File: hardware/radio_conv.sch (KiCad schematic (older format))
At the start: 13 parts

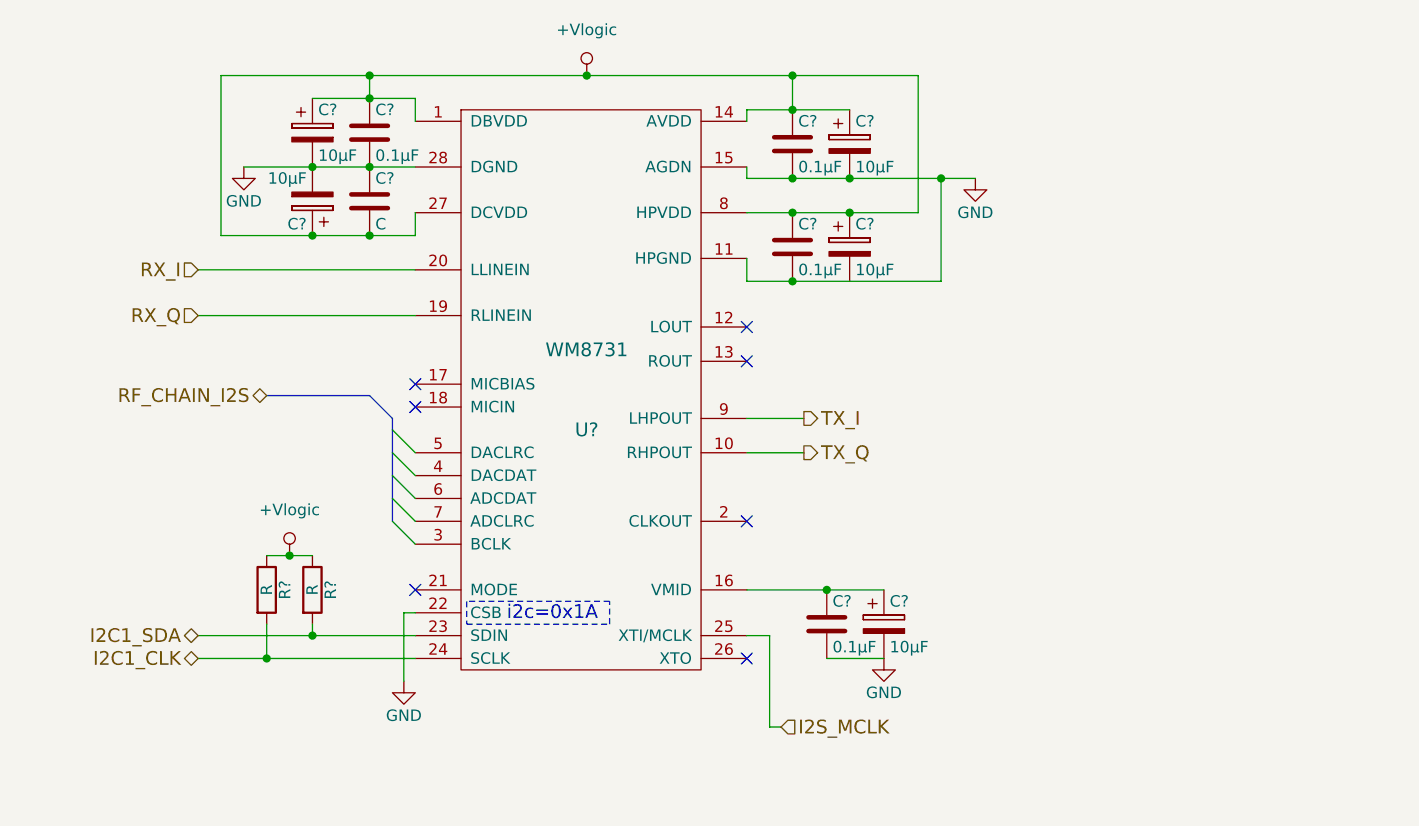
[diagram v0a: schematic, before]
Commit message: Added biases for RX and TX chains where needed
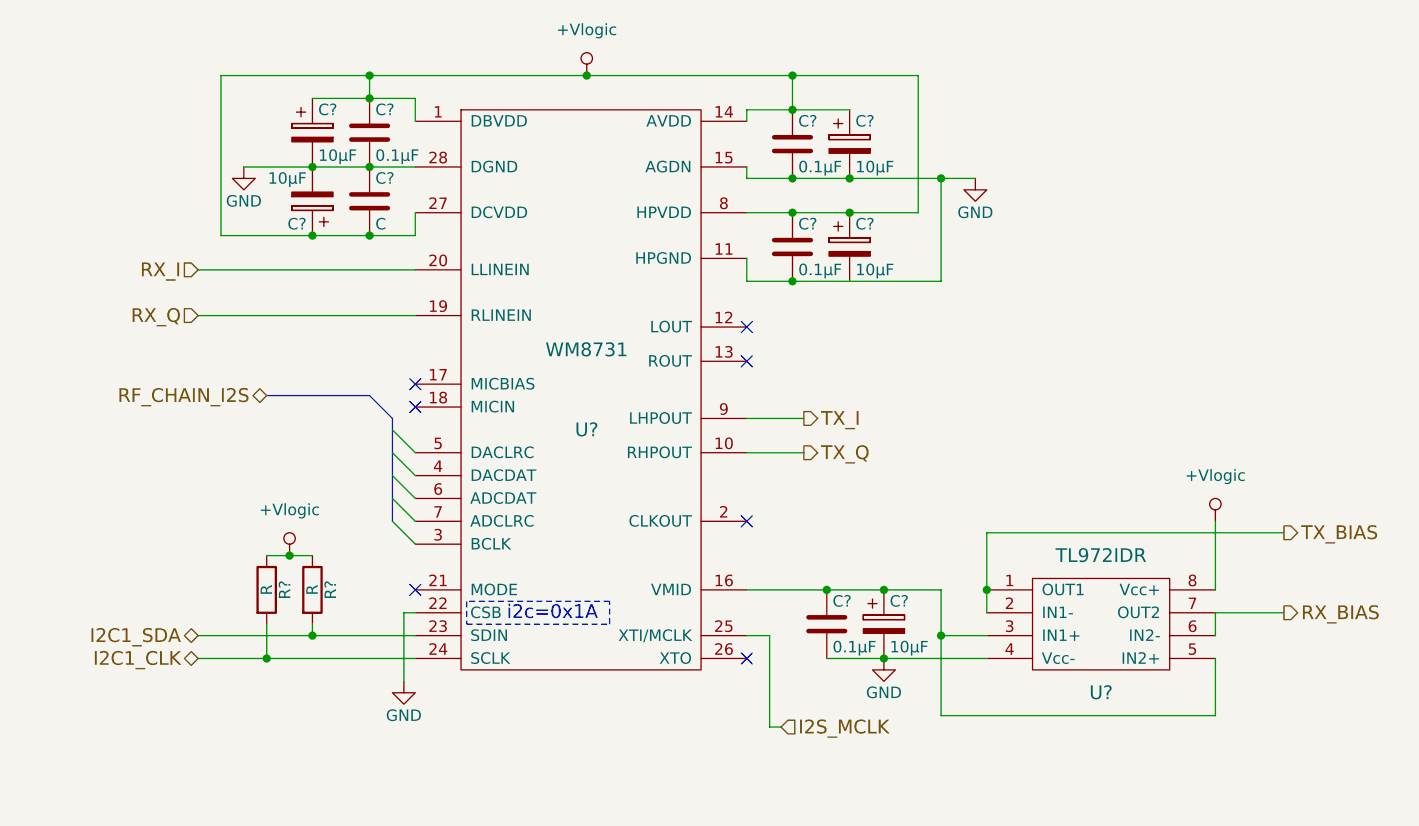
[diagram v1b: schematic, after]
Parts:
- added U?: TL972IDR, symbol TL972IDR
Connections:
- net +Vlogic: now also U?.8 (Vcc+)
- net GND: now also U?.4 (Vcc-)
- net at C?.1, C?.1, U?.16 (VMID): now also U?.3 (IN1+), U?.5 (IN2+)
- new net RX_BIAS: U?.6 (IN2-), U?.7 (OUT2)
- new net TX_BIAS: U?.1 (OUT1), U?.2 (IN1-)
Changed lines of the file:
@@
 Comp "PRK - OH2TI"
 Comment1 "exla - OH2EHK"
-Comment2 ""
+Comment2 "tejeez - OH2EAT"
 Comment3 ""
 Comment4 ""
@@
 $EndComp
 Wire Wire Line
-	4300 2600 4600 2600
-Wire Wire Line
-	4600 2600 4850 2600
-Wire Wire Line
-	4850 2600 5050 2600
+	4300 2600 5050 2600
 Wire Wire Line
 	5050 2300 5050 2400
 Wire Wire Line
-	4600 2300 4850 2300
-Wire Wire Line
-	4850 2300 5050 2300
+	4600 2300 5050 2300
 Connection ~ 4850 2300
 Wire Wire Line
 	4850 2300 4850 2200
 Wire Wire Line
-	4200 2200 4850 2200
-Wire Wire Line
-	4850 2200 5800 2200
-Wire Wire Line
-	5800 2200 6700 2200
-Wire Wire Line
-	6700 2200 7250 2200
+	4200 2200 7250 2200
 Connection ~ 4600 2600
 Connection ~ 4850 2600
@@
 Connection ~ 5800 2200
 Wire Wire Line
-	6500 2350 6700 2350
-Wire Wire Line
-	6700 2350 6950 2350
+	6500 2350 6950 2350
 Wire Wire Line
 	6500 2350 6500 2400
 Connection ~ 6700 2350
 Wire Wire Line
-	6500 2650 6700 2650
-Wire Wire Line
-	6700 2650 6950 2650
-Wire Wire Line
-	6950 2650 7350 2650
-Wire Wire Line
-	7350 2650 7500 2650
+	6500 2650 7500 2650
 Wire Wire Line
 	6500 2650 6500 2600
@@
 	7250 2200 7250 2800
 Wire Wire Line
-	7250 2800 6950 2800
-Wire Wire Line
-	6950 2800 6700 2800
-Wire Wire Line
-	6700 2800 6500 2800
+	7250 2800 6500 2800
 Connection ~ 6700 2200
 Connection ~ 6950 2800
@@
 	6500 3000 6500 3100
 Wire Wire Line
-	6500 3100 6700 3100
-Wire Wire Line
-	6700 3100 7350 3100
+	6500 3100 7350 3100
 Wire Wire Line
 	7350 3100 7350 2650
@@
 NoConn ~ 5050 3650
 Wire Wire Line
-	4200 2900 4600 2900
-Wire Wire Line
-	4600 2900 4850 2900
-Wire Wire Line
-	4850 2900 5050 2900
+	4200 2900 5050 2900
 Wire Wire Line
 	5050 2900 5050 2800
@@
 $EndComp
 Wire Wire Line
-	4100 4650 4600 4650
-Wire Wire Line
-	4600 4650 5050 4650
+	4100 4650 5050 4650
 Wire Wire Line
 	4600 4650 4600 4600
 Wire Wire Line
-	4100 4750 4400 4750
-Wire Wire Line
-	4400 4750 5050 4750
+	4100 4750 5050 4750
 Wire Wire Line
 	4400 4750 4400 4600
 Wire Wire Line
-	4400 4300 4500 4300
-Wire Wire Line
-	4500 4300 4600 4300
+	4400 4300 4600 4300
 Connection ~ 4500 4300
 $Comp
@@
 $EndComp
 Wire Wire Line
-	6500 4450 6850 4450
-Wire Wire Line
-	6850 4450 7100 4450
+	6500 4450 7350 4450
 Connection ~ 6850 4450
 Wire Wire Line
-	6850 4750 7100 4750
+	6850 4750 7550 4750
 $Comp
 L GND #PWR043
@@
 	4850 3600 4950 3700
 Wire Bus Line
-	4950 3700 4950 3750
-Wire Bus Line
-	4950 3750 4950 3850
-Wire Bus Line
-	4950 3850 4950 3950
-Wire Bus Line
-	4950 3950 4950 4050
-Wire Bus Line
-	4950 4050 4950 4150
+	4950 3700 4950 4150
 Wire Bus Line
 	4850 3600 4400 3600
@@
 Wire Wire Line
 	6500 3850 6750 3850
+$Comp
+L TL972IDR U?
+U 1 1 57E46913
+P 8050 4600
+F 0 "U?" H 8050 4300 60  0000 C CNN
+F 1 "TL972IDR" H 8050 4900 60  0000 C CNN
+F 2 "" H 8100 4600 60  0001 C CNN
+F 3 "" H 8100 4600 60  0001 C CNN
+	1    8050 4600
+	1    0    0    -1
+$EndComp
+Wire Wire Line
+	7350 4450 7350 5000
+Wire Wire Line
+	7350 4650 7550 4650
+Connection ~ 7100 4450
+Wire Wire Line
+	7350 5000 8550 5000
+Wire Wire Line
+	8550 5000 8550 4750
+Connection ~ 7350 4650
+Connection ~ 7100 4750
+Wire Wire Line
+	7550 4200 7550 4550
+Wire Wire Line
+	8550 4550 8550 4650
+$Comp
+L +Vlogic #PWR?
+U 1 1 57E46B0D
+P 8550 4150
+F 0 "#PWR?" H 8550 3950 50  0001 C CNN
+F 1 "+Vlogic" H 8550 4350 50  0000 C CNN
+F 2 "" H 8550 4150 50  0000 C CNN
+F 3 "" H 8550 4150 50  0000 C CNN
+	1    8550 4150
+	1    0    0    -1
+$EndComp
+Wire Wire Line
+	8550 4150 8550 4450
+Text HLabel 8850 4550 2    60   Output ~ 0
+RX_BIAS
+Text HLabel 8850 4200 2    60   Output ~ 0
+TX_BIAS
+Wire Wire Line
+	7550 4200 8850 4200
+Connection ~ 7550 4450
+Wire Wire Line
+	8550 4550 8850 4550
 $EndSCHEMATC

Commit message: Added initial CPU block and fixed bugs from other sheets
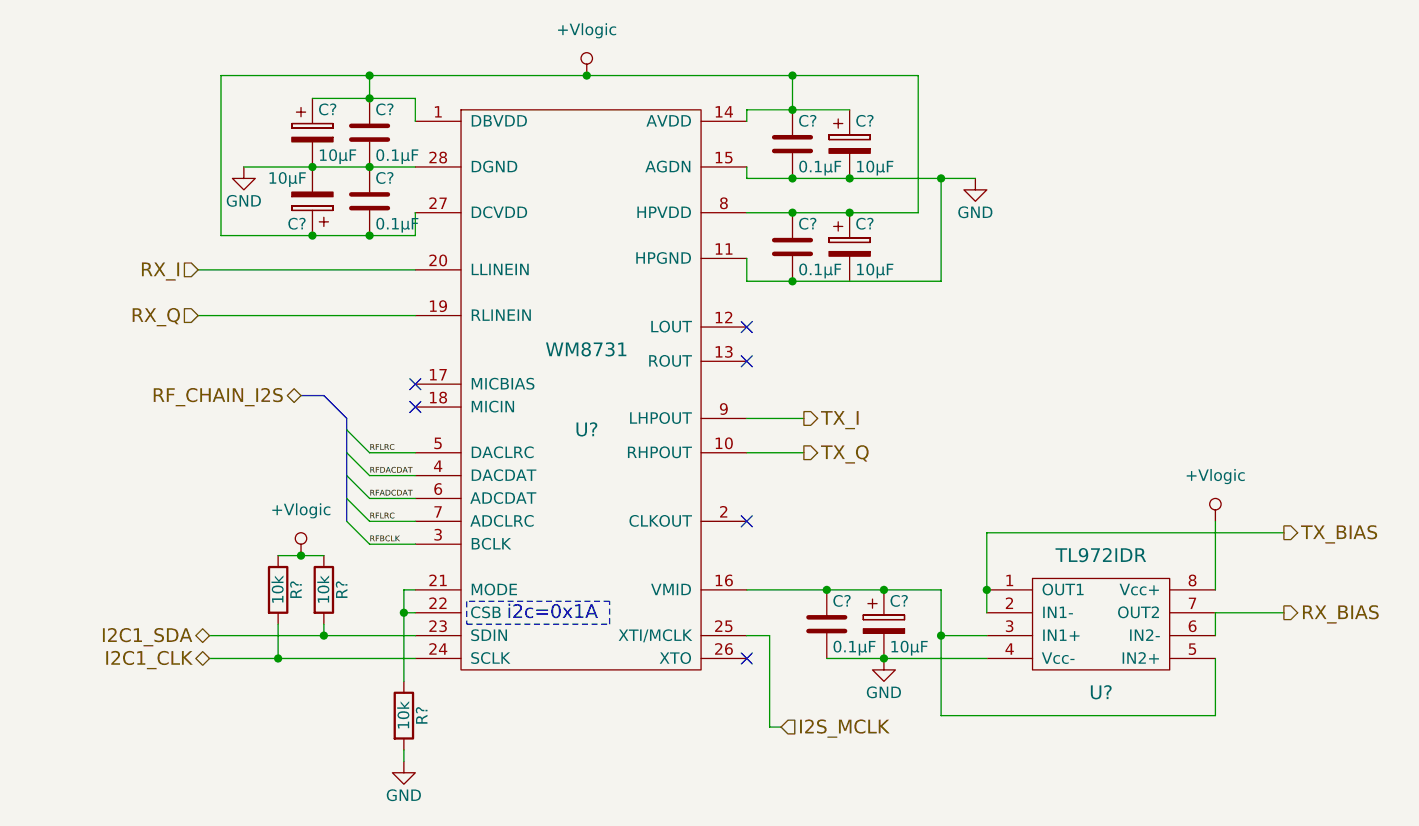
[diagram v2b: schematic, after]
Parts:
- added R?: 10k, symbol R
- C?: value C -> 0.1µF
- R? (x2): value R -> 10k
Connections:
- net GND: now also R?.2; no longer U?.22 (CSB)
- net at U?.21 (MODE): now also U?.22 (CSB), R?.1
- net RFBCLK: now reaches U?.3 (BCLK)
- net RFDACDAT: now reaches U?.4 (DACDAT)
- net RFLRC: now reaches U?.5 (DACLRC)
- net RFLRC: now also U?.7 (ADCLRC)
- net RFADCDAT: now reaches U?.6 (ADCDAT)
- no-connect marks 7 -> 6
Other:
- moved on the sheet: R?
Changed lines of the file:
@@
 LIBS:dodekaedri
 LIBS:Oscillators
+LIBS:stm32
 LIBS:dodekaedri-cache
 EELAYER 25 0
@@
 $Descr A4 11693 8268
 encoding utf-8
-Sheet 7 7
+Sheet 7 8
 Title "RF chain ADC/DAC"
 Date "2016-09-23"
-Rev "0.1"
+Rev "0.4"
 Comp "PRK - OH2TI"
 Comment1 "exla - OH2EHK"
@@
 P 4850 2750
 F 0 "C?" H 4875 2850 50  0000 L CNN
-F 1 "C" H 4875 2650 50  0000 L CNN
+F 1 "0.1µF" H 4875 2650 50  0000 L CNN
 F 2 "" H 4888 2600 50  0000 C CNN
 F 3 "" H 4850 2750 50  0000 C CNN
@@
 $EndComp
 Wire Wire Line
-	4300 2600 5050 2600
+	4300 2600 4600 2600
+Wire Wire Line
+	4600 2600 4850 2600
+Wire Wire Line
+	4850 2600 5050 2600
 Wire Wire Line
 	5050 2300 5050 2400
 Wire Wire Line
-	4600 2300 5050 2300
+	4600 2300 4850 2300
+Wire Wire Line
+	4850 2300 5050 2300
 Connection ~ 4850 2300
 Wire Wire Line
 	4850 2300 4850 2200
 Wire Wire Line
-	4200 2200 7250 2200
+	4200 2200 4850 2200
+Wire Wire Line
+	4850 2200 5800 2200
+Wire Wire Line
+	5800 2200 6700 2200
+Wire Wire Line
+	6700 2200 7250 2200
 Connection ~ 4600 2600
 Connection ~ 4850 2600
@@
 Connection ~ 5800 2200
 Wire Wire Line
-	6500 2350 6950 2350
+	6500 2350 6700 2350
+Wire Wire Line
+	6700 2350 6950 2350
 Wire Wire Line
 	6500 2350 6500 2400
 Connection ~ 6700 2350
 Wire Wire Line
-	6500 2650 7500 2650
+	6500 2650 6700 2650
+Wire Wire Line
+	6700 2650 6950 2650
+Wire Wire Line
+	6950 2650 7350 2650
+Wire Wire Line
+	7350 2650 7500 2650
 Wire Wire Line
 	6500 2650 6500 2600
@@
 $EndComp
 Wire Wire Line
-	7250 2200 7250 2800
-Wire Wire Line
-	7250 2800 6500 2800
+	7250 2800 7250 2200
+Wire Wire Line
+	6500 2800 6700 2800
+Wire Wire Line
+	6700 2800 6950 2800
+Wire Wire Line
+	6950 2800 7250 2800
 Connection ~ 6700 2200
 Connection ~ 6950 2800
@@
 	6500 3000 6500 3100
 Wire Wire Line
-	6500 3100 7350 3100
+	6500 3100 6700 3100
+Wire Wire Line
+	6700 3100 7350 3100
 Wire Wire Line
 	7350 3100 7350 2650
@@
 NoConn ~ 5050 3650
 Wire Wire Line
-	4200 2900 5050 2900
+	4200 2900 4600 2900
+Wire Wire Line
+	4600 2900 4850 2900
+Wire Wire Line
+	4850 2900 5050 2900
 Wire Wire Line
 	5050 2900 5050 2800
@@
 L +Vlogic #PWR042
 U 1 1 57E4C199
-P 4500 4300
-F 0 "#PWR042" H 4500 4100 50  0001 C CNN
-F 1 "+Vlogic" H 4500 4500 50  0000 C CNN
-F 2 "" H 4500 4300 50  0000 C CNN
-F 3 "" H 4500 4300 50  0000 C CNN
-	1    4500 4300
+P 4550 4300
+F 0 "#PWR042" H 4550 4100 50  0001 C CNN
+F 1 "+Vlogic" H 4550 4500 50  0000 C CNN
+F 2 "" H 4550 4300 50  0000 C CNN
+F 3 "" H 4550 4300 50  0000 C CNN
+	1    4550 4300
 	1    0    0    -1
 $EndComp
@@
 L R R?
 U 1 1 57E4C19F
-P 4400 4450
-F 0 "R?" V 4480 4450 50  0000 C CNN
-F 1 "R" V 4400 4450 50  0000 C CNN
-F 2 "" V 4330 4450 50  0000 C CNN
-F 3 "" H 4400 4450 50  0000 C CNN
-	1    4400 4450
+P 4450 4450
+F 0 "R?" V 4530 4450 50  0000 C CNN
+F 1 "10k" V 4450 4450 50  0000 C CNN
+F 2 "" V 4380 4450 50  0000 C CNN
+F 3 "" H 4450 4450 50  0000 C CNN
+	1    4450 4450
 	1    0    0    -1
 $EndComp
@@
 L R R?
 U 1 1 57E4C1A6
-P 4600 4450
-F 0 "R?" V 4680 4450 50  0000 C CNN
-F 1 "R" V 4600 4450 50  0000 C CNN
-F 2 "" V 4530 4450 50  0000 C CNN
-F 3 "" H 4600 4450 50  0000 C CNN
-	1    4600 4450
-	1    0    0    -1
-$EndComp
-Wire Wire Line
-	4100 4650 5050 4650
-Wire Wire Line
-	4600 4650 4600 4600
-Wire Wire Line
-	4100 4750 5050 4750
-Wire Wire Line
-	4400 4750 4400 4600
-Wire Wire Line
-	4400 4300 4600 4300
-Connection ~ 4500 4300
+P 4650 4450
+F 0 "R?" V 4730 4450 50  0000 C CNN
+F 1 "10k" V 4650 4450 50  0000 C CNN
+F 2 "" V 4580 4450 50  0000 C CNN
+F 3 "" H 4650 4450 50  0000 C CNN
+	1    4650 4450
+	1    0    0    -1
+$EndComp
+Wire Wire Line
+	4150 4650 4650 4650
+Wire Wire Line
+	4650 4650 5050 4650
+Wire Wire Line
+	4650 4650 4650 4600
+Wire Wire Line
+	4150 4750 4450 4750
+Wire Wire Line
+	4450 4750 5050 4750
+Wire Wire Line
+	4450 4750 4450 4600
+Connection ~ 4550 4300
 $Comp
 L C C?
@@
 $EndComp
 Wire Wire Line
-	6500 4450 7350 4450
+	6500 4450 6850 4450
+Wire Wire Line
+	6850 4450 7100 4450
+Wire Wire Line
+	7100 4450 7350 4450
 Connection ~ 6850 4450
 Wire Wire Line
-	6850 4750 7550 4750
+	6850 4750 7100 4750
+Wire Wire Line
+	7100 4750 7550 4750
 $Comp
 L GND #PWR043
@@
 $EndComp
 Entry Wire Line
-	4950 4150 5050 4250
+	4750 4150 4850 4250
 Entry Wire Line
-	4950 4050 5050 4150
+	4750 4050 4850 4150
 Entry Wire Line
-	4950 3950 5050 4050
+	4750 3950 4850 4050
 Entry Wire Line
-	4950 3850 5050 3950
+	4750 3850 4850 3950
 Entry Wire Line
-	4950 3750 5050 3850
-Text HLabel 4400 3600 0    60   BiDi ~ 0
+	4750 3750 4850 3850
+Text HLabel 4550 3600 0    60   BiDi ~ 0
 RF_CHAIN_I2S
 Wire Bus Line
-	4850 3600 4950 3700
-Wire Bus Line
-	4950 3700 4950 4150
-Wire Bus Line
-	4850 3600 4400 3600
-Text HLabel 4100 4650 0    60   BiDi ~ 0
+	4650 3600 4750 3700
+Wire Bus Line
+	4750 3700 4750 3750
+Wire Bus Line
+	4750 3750 4750 3850
+Wire Bus Line
+	4750 3850 4750 3950
+Wire Bus Line
+	4750 3950 4750 4050
+Wire Bus Line
+	4750 4050 4750 4150
+Wire Bus Line
+	4650 3600 4550 3600
+Text HLabel 4150 4650 0    60   BiDi ~ 0
 I2C1_SDA
-Connection ~ 4600 4650
-Text HLabel 4100 4750 0    60   BiDi ~ 0
+Connection ~ 4650 4650
+Text HLabel 4150 4750 0    60   BiDi ~ 0
 I2C1_CLK
-Connection ~ 4400 4750
+Connection ~ 4450 4750
 Text HLabel 6650 5050 2    60   Input ~ 0
 I2S_MCLK
@@
 Text HLabel 4100 3250 0    60   Input ~ 0
 RX_Q
-NoConn ~ 5050 4450
 $Comp
 L GND #PWR044
 U 1 1 57E4C1DF
-P 5000 4850
-F 0 "#PWR044" H 5000 4600 50  0001 C CNN
-F 1 "GND" H 5000 4700 50  0000 C CNN
-F 2 "" H 5000 4850 50  0000 C CNN
-F 3 "" H 5000 4850 50  0000 C CNN
-	1    5000 4850
+P 5000 5200
+F 0 "#PWR044" H 5000 4950 50  0001 C CNN
+F 1 "GND" H 5000 5050 50  0000 C CNN
+F 2 "" H 5000 5200 50  0000 C CNN
+F 3 "" H 5000 5200 50  0000 C CNN
+	1    5000 5200
 	1    0    0    -1
 $EndComp
 Wire Wire Line
 	5050 4550 5000 4550
+Wire Wire Line
+	5000 4450 5000 4550
 Wire Wire Line
 	5000 4550 5000 4850
@@
 $EndComp
 Wire Wire Line
-	7350 4450 7350 5000
+	7350 4450 7350 4650
+Wire Wire Line
+	7350 4650 7350 5000
 Wire Wire Line
 	7350 4650 7550 4650
@@
 Connection ~ 7100 4750
 Wire Wire Line
-	7550 4200 7550 4550
+	7550 4200 7550 4450
+Wire Wire Line
+	7550 4450 7550 4550
 Wire Wire Line
 	8550 4550 8550 4650
@@
 Wire Wire Line
 	8550 4550 8850 4550
+Wire Wire Line
+	5050 3850 4850 3850
+Wire Wire Line
+	5050 3950 4850 3950
+Wire Wire Line
+	5050 4050 4850 4050
+Wire Wire Line
+	5050 4150 4850 4150
+Wire Wire Line
+	5050 4250 4850 4250
+Connection ~ 5000 4550
+Wire Wire Line
+	4450 4300 4550 4300
+Wire Wire Line
+	4550 4300 4650 4300
+Wire Wire Line
+	5000 4450 5050 4450
+Text Label 4850 3850 0    25   ~ 0
+RFLRC
+Text Label 4850 4150 0    25   ~ 0
+RFLRC
+Text Label 4850 3950 0    25   ~ 0
+RFDACDAT
+Text Label 4850 4050 0    25   ~ 0
+RFADCDAT
+Text Label 4850 4250 0    25   ~ 0
+RFBCLK
+$Comp
+L R R?
+U 1 1 57E786C6
+P 5000 5000
+F 0 "R?" V 5080 5000 50  0000 C CNN
+F 1 "10k" V 5000 5000 50  0000 C CNN
+F 2 "" V 4930 5000 50  0000 C CNN
+F 3 "" H 5000 5000 50  0000 C CNN
+	1    5000 5000
+	1    0    0    -1
+$EndComp
+Wire Wire Line
+	5000 5200 5000 5150
 $EndSCHEMATC
